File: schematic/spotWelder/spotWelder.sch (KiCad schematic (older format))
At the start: 28 parts, among them J1 InterBoard, Q1 Q_NPN_BCE, SW1 Rotary_Encoder_Switch, U1 BLUEPILL-STM32F103CBTx, U3 DC/DC converter

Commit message: update pinout
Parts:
- Brd?: symbol SSD1306-128x64_OLED:SSD1306 -> spotWelder-rescue:SSD1306-SSD1306-128x64_OLED
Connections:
- net at U1.22 (PB11): now also SW1.S1
- net at U1.29 (PA8): no longer SW1.S1
- net at U1.30 (PA9): no longer SW1.A
- net at U1.31 (PA10): no longer SW1.B
- net at U1.45 (PB8): now also SW1.B
- net at U1.46 (PB9): now also SW1.A
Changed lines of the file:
@@
 	4850 4950 5000 4950
 Wire Wire Line
-	3100 4300 4750 4300
-Wire Wire Line
-	4750 4300 4750 4850
-Wire Wire Line
 	4750 4850 5000 4850
-Wire Wire Line
-	3100 4400 4300 4400
-Wire Wire Line
-	4300 4400 4300 5250
-Wire Wire Line
-	4300 5250 5000 5250
-Wire Wire Line
-	5000 5250 5000 5050
-Wire Wire Line
-	3100 4200 5850 4200
-Wire Wire Line
-	5850 4200 5850 4850
 Wire Wire Line
 	5850 4850 5600 4850
@@
 Put near PA3 to avoid buzzer/I2C parasites
 $Comp
-L SSD1306-128x64_OLED:SSD1306 Brd?
+L spotWelder-rescue:SSD1306-SSD1306-128x64_OLED Brd?
 U 1 1 606A4189
 P 4050 1650
@@
 	3500 5600 3500 6750
 Connection ~ 3500 6750
+Wire Wire Line
+	1800 4200 1700 4200
+Wire Wire Line
+	1700 4200 1700 5500
+Wire Wire Line
+	1700 5500 5000 5500
+Wire Wire Line
+	5000 5050 5000 5500
+Wire Wire Line
+	1800 4300 1750 4300
+Wire Wire Line
+	1750 4300 1750 5400
+Wire Wire Line
+	1750 5400 4750 5400
+Wire Wire Line
+	4750 5400 4750 4850
+Wire Wire Line
+	1800 4500 2700 4500
+Wire Wire Line
+	2700 4500 2700 5150
+Wire Wire Line
+	2700 5150 4500 5150
+Wire Wire Line
+	4500 5150 4500 4350
+Wire Wire Line
+	4500 4350 5850 4350
+Wire Wire Line
+	5850 4350 5850 4850
 $EndSCHEMATC

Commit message: sync
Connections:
- net at U1.17 (PA7): no longer D?.4 (DIN)
- net at U1.39 (PB3): now also D?.4 (DIN)
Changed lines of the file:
@@
 	6800 1450 7100 1450
-Wire Wire Line
-	3100 4100 3300 4100
-Wire Wire Line
-	3300 4100 3300 2950
-Wire Wire Line
-	3300 2950 3950 2950
-Wire Wire Line
-	3950 2950 3950 2400
-Wire Wire Line
-	3950 2400 4900 2400
-Wire Wire Line
-	4900 2400 4900 1450
 Wire Wire Line
 	4900 1450 5300 1450
@@
 Wire Wire Line
 	5850 4350 5850 4850
+Wire Wire Line
+	4900 1450 4900 850
+Wire Wire Line
+	4900 850  950  850
+Wire Wire Line
+	950  850  950  3700
+Wire Wire Line
+	950  3700 1800 3700
+Text Label 750  3200 0    50   ~ 0
+PB3
 $EndSCHEMATC

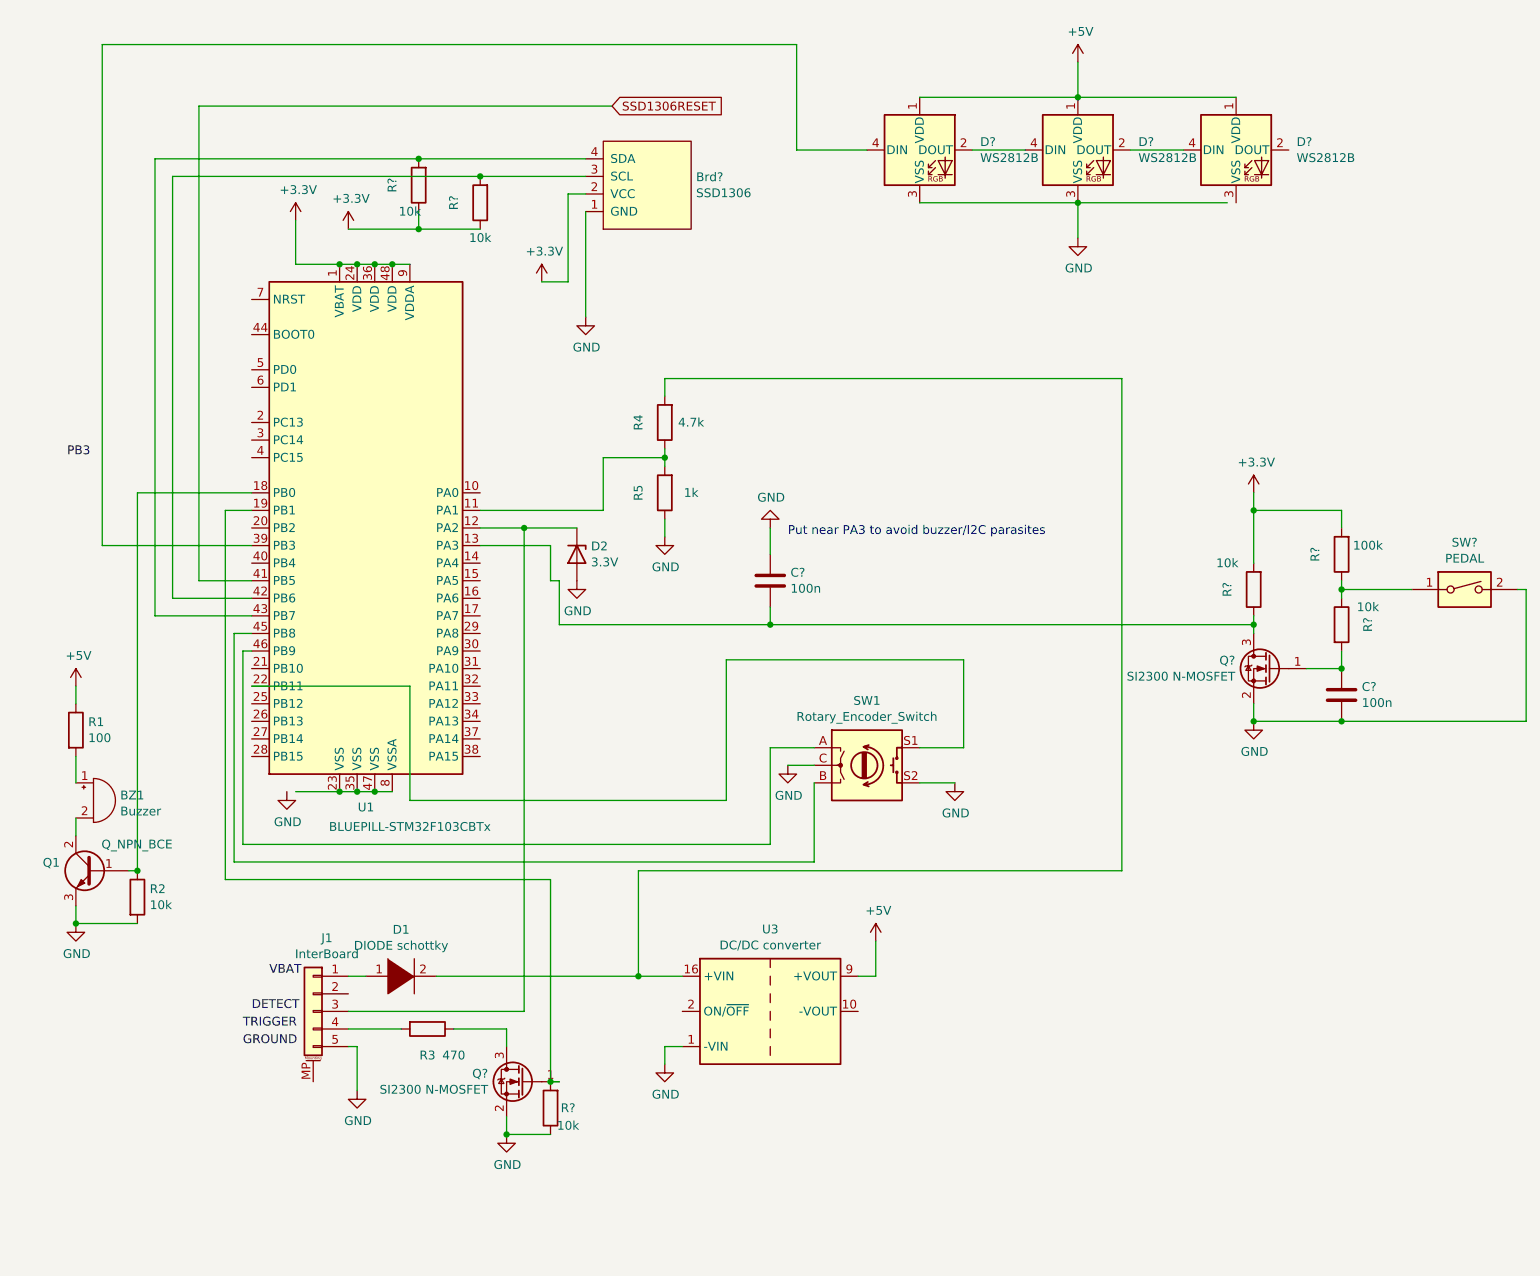
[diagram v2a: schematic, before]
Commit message: update schematic
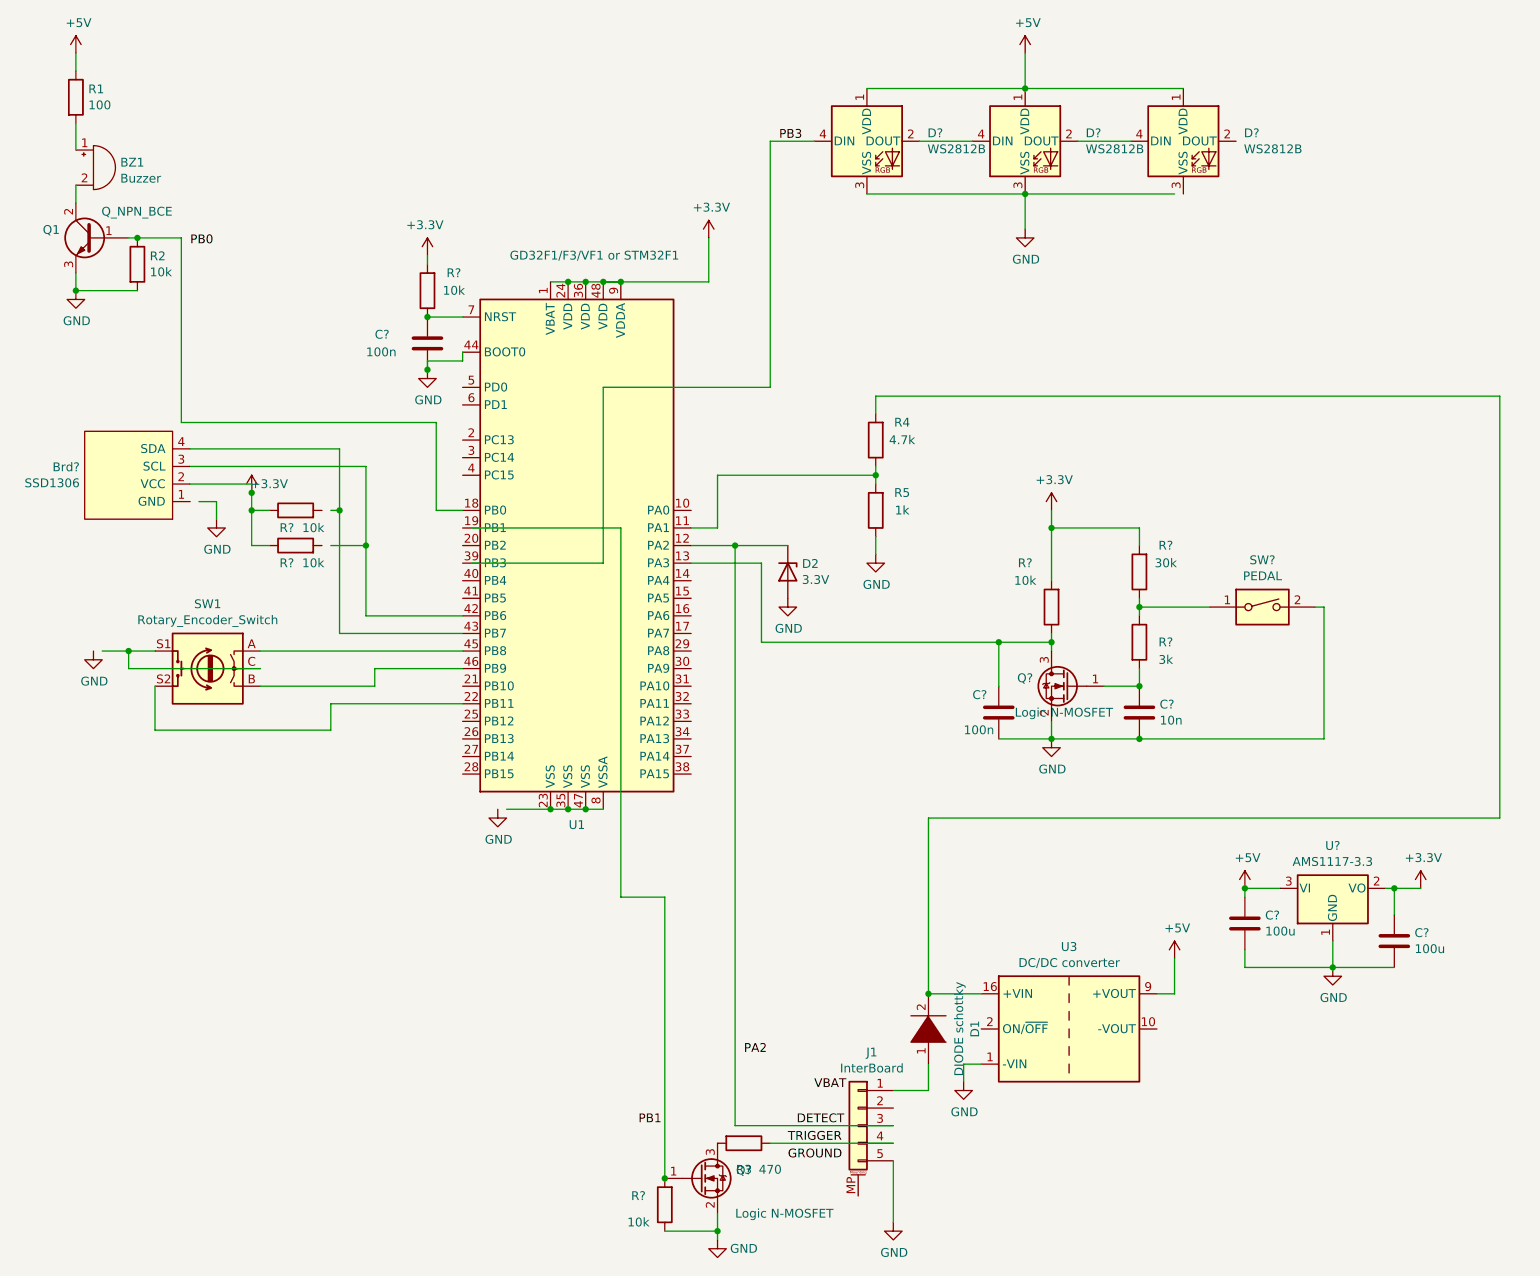
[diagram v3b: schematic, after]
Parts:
- removed R? (x2): 10k, symbol Device:R
- added C? (x2): 100u, symbol Device:C
- added C?: 100n, symbol Device:C
- added R? (x3): 10k, symbol Device:R
- added U?: AMS1117-3.3, Package_TO_SOT_SMD:SOT-223-3_TabPin2, symbol Regulator_Linear:AMS1117-3.3
- C?: value 100n -> 10n
- Q? (x2): value SI2300 N-MOSFET -> Logic N-MOSFET
- R?: value 10k -> 3k
- R?: value 100k -> 30k
- U1: value BLUEPILL-STM32F103CBTx -> GD32F1/F3/VF1 or STM32F1
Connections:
- net labels added: PA2, PB0, PB1
- net labels removed: SSD1306RESET
- wire segments 125 -> 132
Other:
- note removed: "Put near PA3 to avoid buzzer/I2C parasites"
- moved on the sheet: BZ1, Brd?, C?, D1, D2, D?, J1, Q1, Q?, R1, R2, R3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

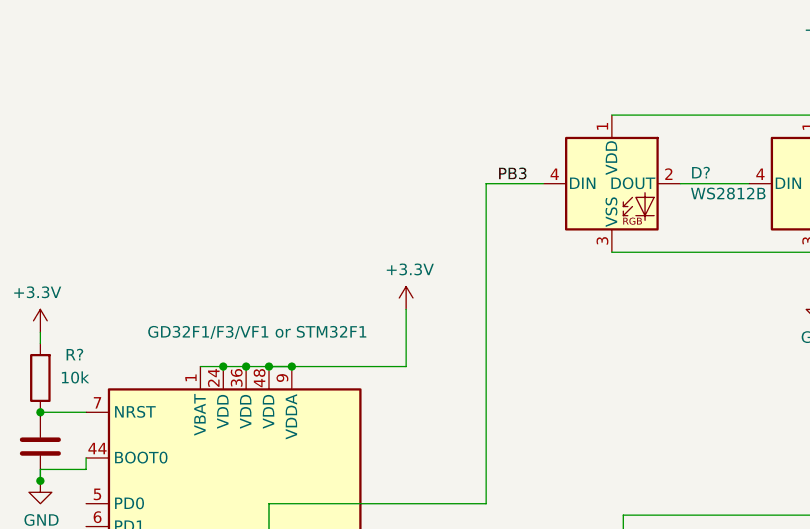
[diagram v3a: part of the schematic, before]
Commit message: add info about using PB10 instead of PB3 for the VF103
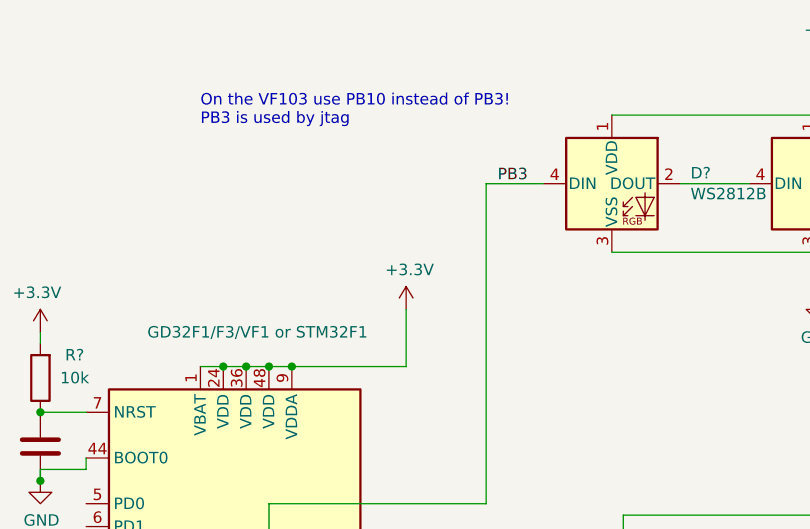
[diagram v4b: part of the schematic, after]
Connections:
- wire segments 132 -> 131
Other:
- note added: "On the VF103 use PB10 instead of PB3!\nPB3 is used by jtag"
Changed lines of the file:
@@
 $EndComp
-Wire Wire Line
-	3800 2200 3900 2200
 Wire Wire Line
 	4400 2200 4400 1950
@@
 Wire Wire Line
 	3900 2200 4400 2200
+Text Notes 3500 1150 0    50   ~ 0
+On the VF103 use PB10 instead of PB3!\nPB3 is used by jtag
 $EndSCHEMATC
